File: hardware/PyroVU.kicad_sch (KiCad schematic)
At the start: 4 parts, among them J1 Screw_Terminal_01x04, J2 Screw_Terminal_01x02, U1 MAX31856, U2 MAX31865xAP

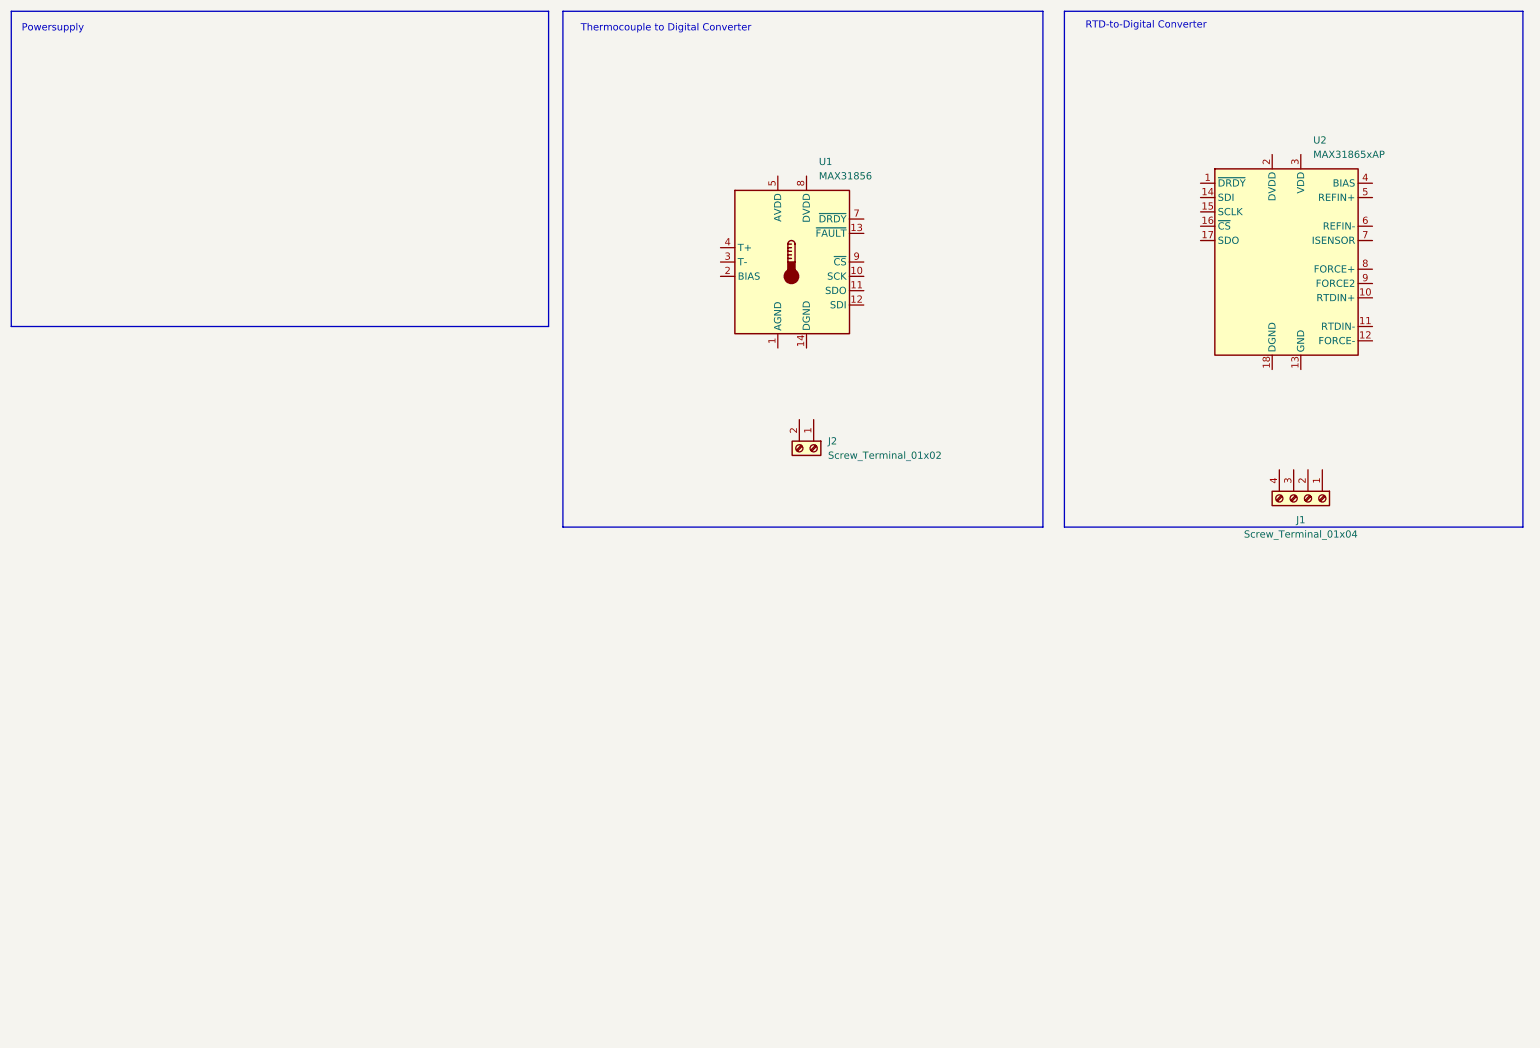
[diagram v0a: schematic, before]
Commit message: Updated schematic added footprints and edited doc file
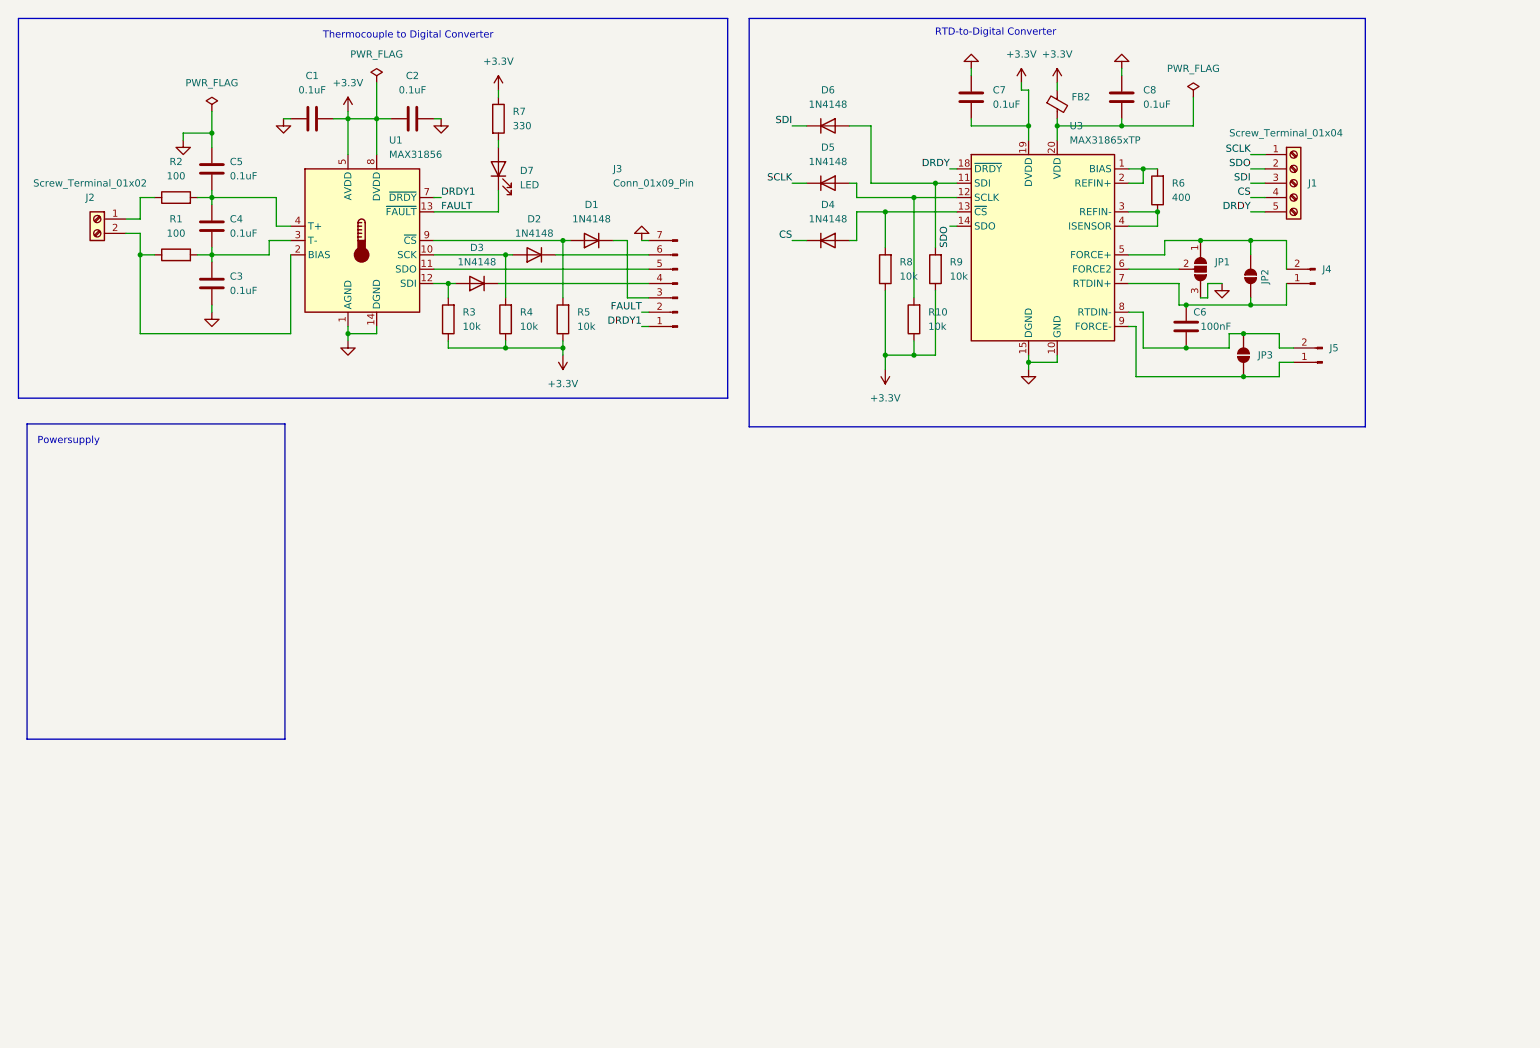
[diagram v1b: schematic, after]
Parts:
- removed U2: MAX31865xAP, Package_SO:SSOP-20_5.3x7.2mm_P0.65mm, symbol Sensor_Temperature:MAX31865xAP
- added C1, C2, C3, C4, C5, C7, C8: 0.1uF, Capacitor_SMD:C_0603_1608Metric, symbol Device:C
- added C6: 100nF, Capacitor_SMD:C_0603_1608Metric, symbol Device:C
- added D1, D2, D3, D4, D5, D6: 1N4148, Diode_THT:D_DO-35_SOD27_P7.62mm_Horizontal, symbol Diode:1N4148
- added D7: LED, LED_SMD:LED_0805_2012Metric, symbol Device:LED
- added FB2: FerriteBead_Small, symbol Device:FerriteBead_Small
- added J3: Conn_01x09_Pin, symbol Connector:Conn_01x07_Pin
- added J4, J5: Conn_01x02_Pin, symbol Connector:Conn_01x02_Pin
- added JP1: SolderJumper_3_Open, symbol Jumper:SolderJumper_3_Open
- added JP2, JP3: SolderJumper_2_Open, symbol Jumper:SolderJumper_2_Open
- added R1, R2: 100, Resistor_SMD:R_0805_2012Metric, symbol Device:R
- added R10, R3, R4, R5, R8, R9: 10k, Resistor_SMD:R_0805_2012Metric, symbol Device:R
- added R6: 400, Resistor_SMD:R_0805_2012Metric, symbol Device:R
- added R7: 330, Resistor_SMD:R_0805_2012Metric, symbol Device:R
- added U3: MAX31865xTP, Package_DFN_QFN:TQFN-20-1EP_5x5mm_P0.65mm_EP3.25x3.25mm, symbol Sensor_Temperature:MAX31865xTP
- J1: symbol Connector:Screw_Terminal_01x04 -> Connector:Screw_Terminal_01x05
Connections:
- net at J2.1 (Pin_1): now also R2.1
- net at J2.2 (Pin_2): now also U1.2 (BIAS), R1.1
- net SCLK: now reaches J1.1 (Pin_1)
- net SCLK: now also D5.1 (K)
- net SDO: now reaches J1.2 (Pin_2)
- net SDO: now also U3.14 (SDO)
- net SDI: now reaches J1.3 (Pin_3)
- net SDI: now also D6.1 (K)
- net CS: now reaches J1.4 (Pin_4)
- net CS: now also D4.1 (K)
- net GND: now reaches U1.1 (AGND)
- net GND: now also U1.14 (DGND), C1.1, C2.2, C3.1, C5.2, C7.1, C8.1, J3.7 (Pin_7), JP1.3 (B), U3.10 (GND), U3.15 (DGND), U3.16 (GND), U3.21 (GND)
- net at U1.10 (SCK): now also D2.2 (A), R4.2
- net at U1.11 (SDO): now also J3.5 (Pin_5)
- net at U1.12 (SDI): now also D3.2 (A), R3.2
- net FAULT: now reaches U1.13 (~{FAULT})
- net FAULT: now also D7.1 (K), J3.2 (Pin_2)
- net at U1.3 (T-): now also C3.2, C4.1, R1.2
- net at U1.4 (T+): now also C4.2, C5.1, R2.2
- net +3.3V: now reaches U1.5 (AVDD)
- net +3.3V: now also U1.8 (DVDD), C1.2, C2.1, C7.2, FB2.1, R10.1, R3.1, R4.1, R5.1, R7.1, R8.1, R9.1, U3.19 (DVDD)
- net DRDY1: now reaches U1.7 (~{DRDY})
- net DRDY1: now also J3.1 (Pin_1)
- net at U1.9 (~{CS}): now also D1.2 (A), R5.2
- new net: C6.1, J4.1 (Pin_1), JP2.1 (A), U3.7 (RTDIN+)
- new net: J4.2 (Pin_2), JP1.1 (A), JP2.2 (B), U3.5 (FORCE+)
- new net: D6.2 (A), R9.2, U3.11 (SDI)
- new net: D4.2 (A), R8.2, U3.13 (~{CS})
- new net: J5.1 (Pin_1), JP3.1 (A), U3.9 (FORCE-)
- new net: C6.2, J5.2 (Pin_2), JP3.2 (B), U3.8 (RTDIN-)
- new net: C8.2, FB2.2, U3.20 (VDD)
- new net: D1.1 (K), J3.3 (Pin_3)
- new net: D5.2 (A), R10.2, U3.12 (SCLK)
- new net: D7.2 (A), R7.2
- new net: JP1.2 (C), U3.6 (FORCE2)
- new net: D3.1 (K), J3.4 (Pin_4)
- new net: D2.1 (K), J3.6 (Pin_6)
- new net: R6.1, U3.3 (REFIN-), U3.4 (ISENSOR)
- new net: R6.2, U3.1 (BIAS), U3.2 (REFIN+)
- new net DRDY: J1.5 (Pin_5), U3.18 (~{DRDY})
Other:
- moved on the sheet: J2, U1

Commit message: Added the new LED driver
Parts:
- added C10, C9: 100pF, Capacitor_SMD:C_0603_1608Metric, symbol Device:C
- added IC1: TM1637__SOP_, SOIC127P1045X280-20N, symbol Custom_symbol:TM1637__SOP_
- added J10, J11, J12, J7, J8, J9: Screw_Terminal_01x09, symbol Connector:Screw_Terminal_01x09
- added J6: Conn_01x02_Pin, symbol Connector:Conn_01x02_Pin
- added R11, R12: 10k, Resistor_SMD:R_0805_2012Metric, symbol Device:R
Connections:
- net +3.3V: now also IC1.16 (VDD), R11.2, R12.2
- net GND: now also C10.1, C9.1, IC1.1 (GND)
- new net: C9.2, IC1.18 (CLK), J6.2 (Pin_2), R11.1
- new net: C10.2, IC1.17 (DIO), J6.1 (Pin_1), R12.1
- new net GRID1: IC1.15 (GRID1), J11.9 (Pin_9)
- new net GRID2: IC1.14 (GRID2), J7.9 (Pin_9)
- new net GRID3: IC1.13 (GRID3), J8.9 (Pin_9)
- new net GRID4: IC1.12 (GRID4), J9.9 (Pin_9)
- new net GRID5: IC1.11 (GRID5), J10.9 (Pin_9)
- new net GRID6: IC1.10 (GRID6), J12.9 (Pin_9)
- new net SEG1: IC1.2 (SEG1/KS1), J10.1 (Pin_1), J11.1 (Pin_1), J12.1 (Pin_1), J7.1 (Pin_1), J8.1 (Pin_1), J9.1 (Pin_1)
- new net SEG2: IC1.3 (SEG2/KS2), J10.2 (Pin_2), J11.2 (Pin_2), J12.2 (Pin_2), J7.2 (Pin_2), J8.2 (Pin_2), J9.2 (Pin_2)
- new net SEG3: IC1.4 (SEG3/KS3), J10.3 (Pin_3), J11.3 (Pin_3), J12.3 (Pin_3), J7.3 (Pin_3), J8.3 (Pin_3), J9.3 (Pin_3)
- new net SEG4: IC1.5 (SEG4/KS4), J10.4 (Pin_4), J11.4 (Pin_4), J12.4 (Pin_4), J7.4 (Pin_4), J8.4 (Pin_4), J9.4 (Pin_4)
- new net SEG5: IC1.6 (SEG5/KS5), J10.5 (Pin_5), J11.5 (Pin_5), J12.5 (Pin_5), J7.5 (Pin_5), J8.5 (Pin_5), J9.5 (Pin_5)
- new net SEG6: IC1.7 (SEG6/KS6), J10.6 (Pin_6), J11.6 (Pin_6), J12.6 (Pin_6), J7.6 (Pin_6), J8.6 (Pin_6), J9.6 (Pin_6)
- new net SEG7: IC1.8 (SEG7/KS7), J10.7 (Pin_7), J11.7 (Pin_7), J12.7 (Pin_7), J7.7 (Pin_7), J8.7 (Pin_7), J9.7 (Pin_7)
- new net SEG8: IC1.9 (SEG8/KS8), J10.8 (Pin_8), J11.8 (Pin_8), J12.8 (Pin_8), J7.8 (Pin_8), J8.8 (Pin_8), J9.8 (Pin_8)
- no-connect marks 0 -> 2

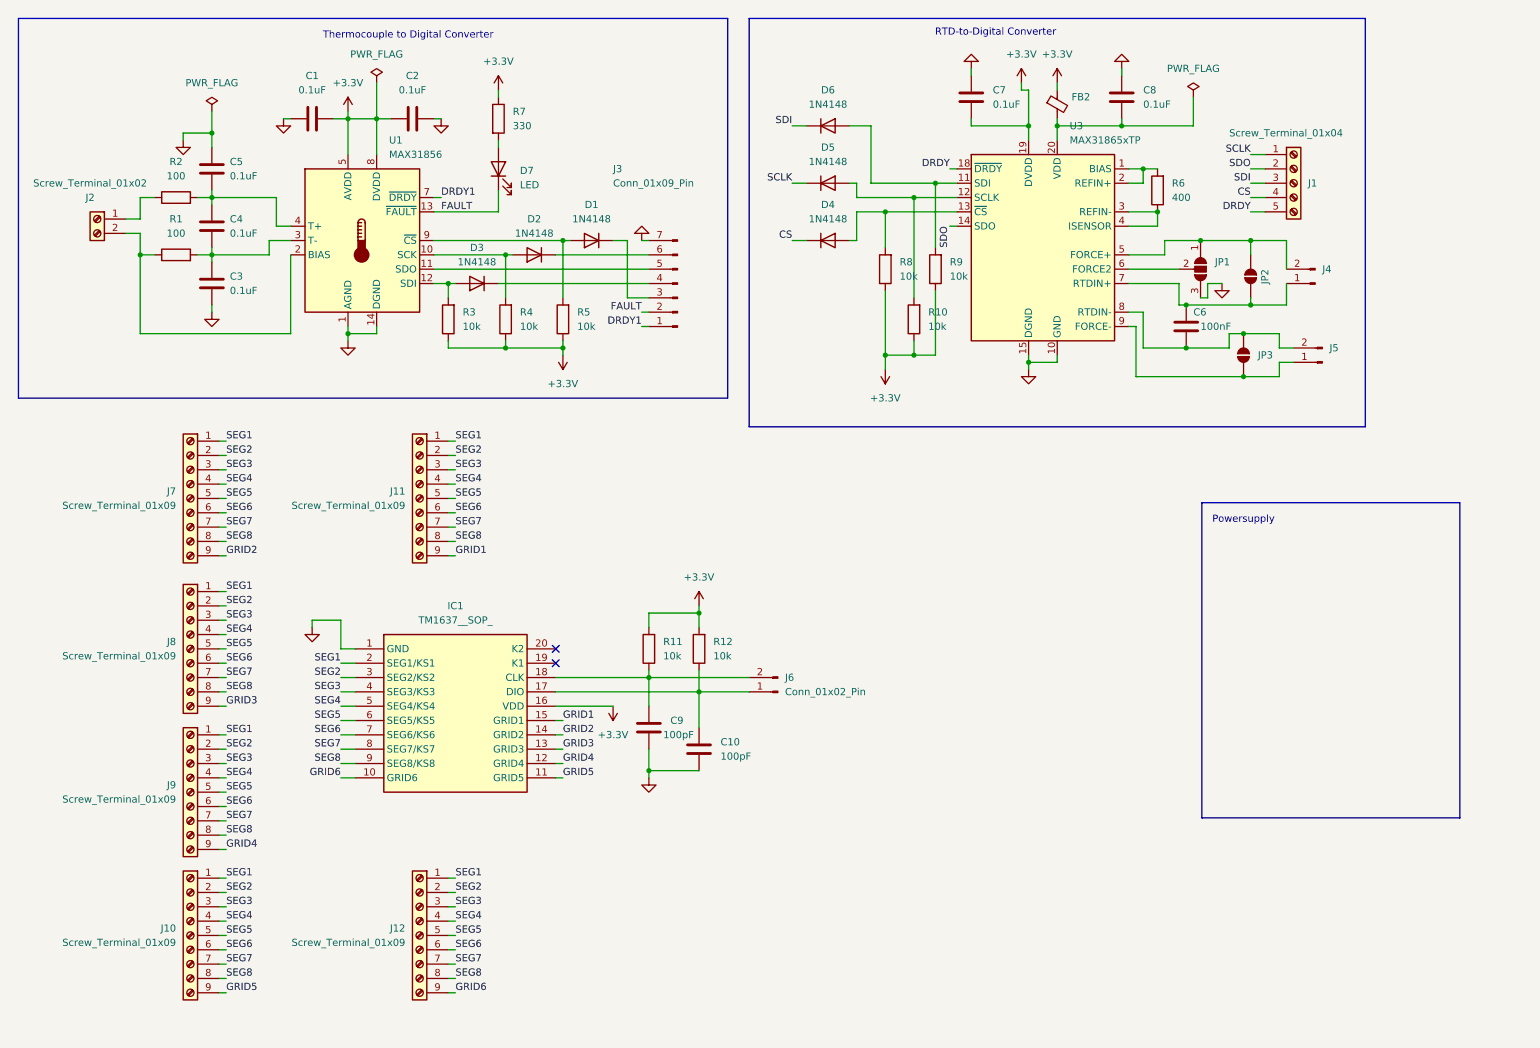
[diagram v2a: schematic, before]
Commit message: Assigned the footprints
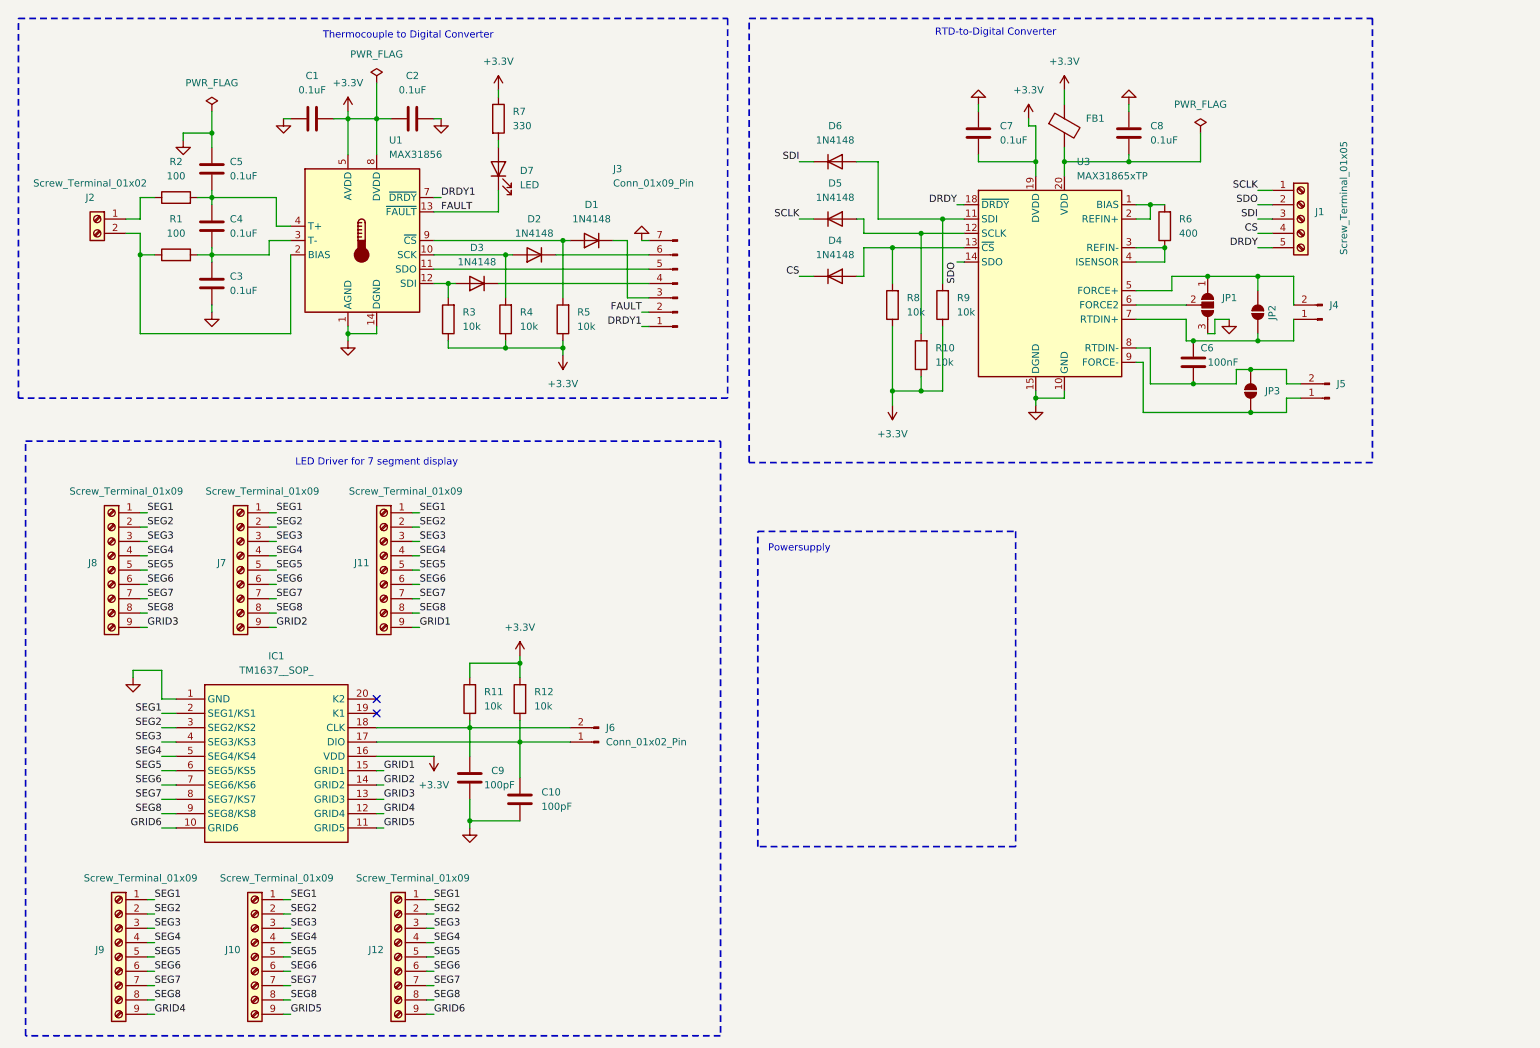
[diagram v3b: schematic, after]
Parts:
- removed FB2: FerriteBead_Small, symbol Device:FerriteBead_Small
- added FB1: FerriteBead, Ferrite_THT:LairdTech_28C0236-0JW-10, symbol Device:FerriteBead
- IC1: footprint SOIC127P1045X280-20N -> Custom_Led_driver_7_segment:SOIC127P1045X280-20N
- J1: value Screw_Terminal_01x04 -> Screw_Terminal_01x05; footprint (none) -> TerminalBlock_Phoenix:TerminalBlock_Phoenix_MPT-0,5-5-2.54_1x05_P2.54mm_Horizontal
- J10, J11, J12, J7, J8, J9: footprint (none) -> TerminalBlock_Phoenix:TerminalBlock_Phoenix_MPT-0,5-9-2.54_1x09_P2.54mm_Horizontal
- J2: footprint (none) -> TerminalBlock_Phoenix:TerminalBlock_Phoenix_MPT-0,5-2-2.54_1x02_P2.54mm_Horizontal
- J3: footprint (none) -> Connector_Molex:Molex_KK-254_AE-6410-07A_1x07_P2.54mm_Vertical
- J4, J5, J6: footprint (none) -> Connector_Molex:Molex_KK-254_AE-6410-02A_1x02_P2.54mm_Vertical
- JP1: footprint (none) -> Jumper:SolderJumper-3_P1.3mm_Open_Pad1.0x1.5mm
- JP2, JP3: footprint (none) -> Jumper:SolderJumper-2_P1.3mm_Open_Pad1.0x1.5mm
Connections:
- net +3.3V: now also FB1.1
- net at C8.2, U3.20 (VDD): now also FB1.2
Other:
- note added: "LED Driver for 7 segment display"
- moved on the sheet: C10, C6, C7, C8, C9, D4, D5, D6, IC1, J10, J11, J12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
